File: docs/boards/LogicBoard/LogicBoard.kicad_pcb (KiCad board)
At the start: 2 copper layers, 50 x 100 mm, 7 parts, among them J1 24V IN, J2 12V OUT, U1 URB2412ZP-6WR3

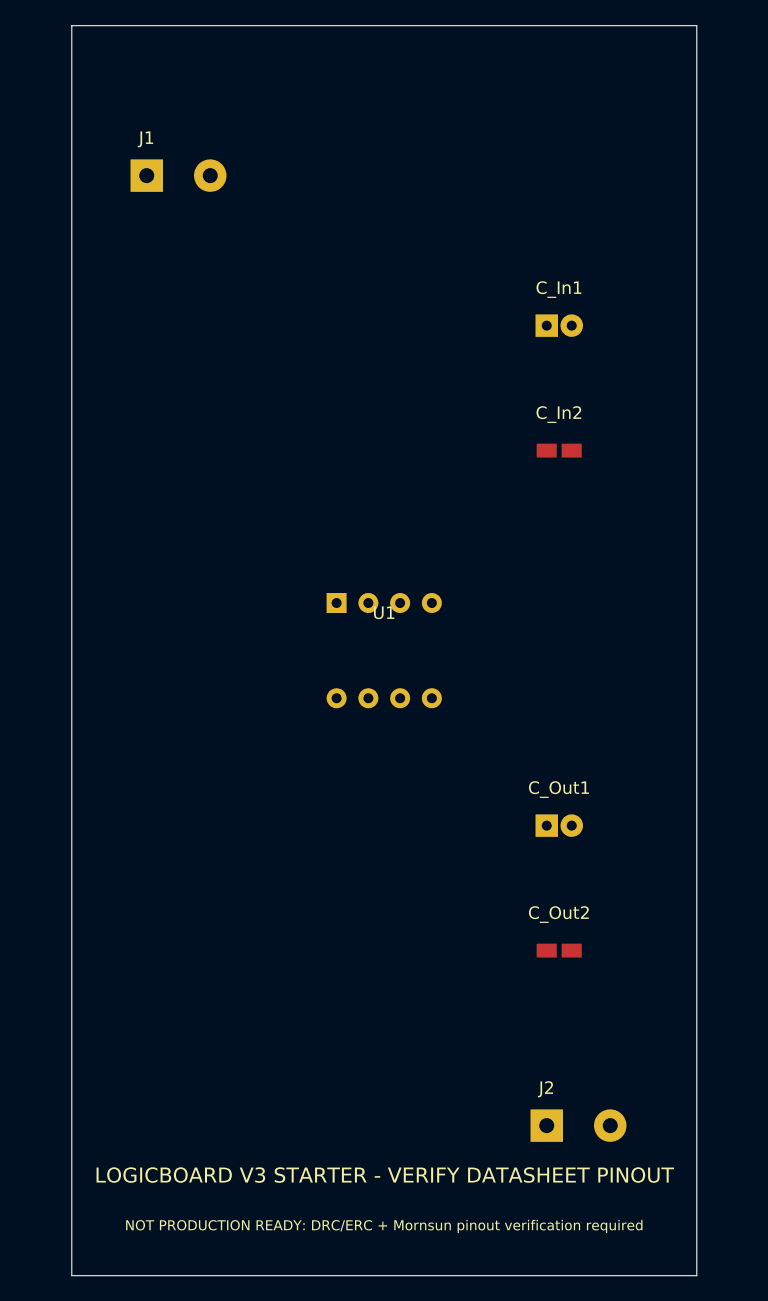
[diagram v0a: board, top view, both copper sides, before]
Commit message: Remake LogicBoard PCB to v4A functional layout
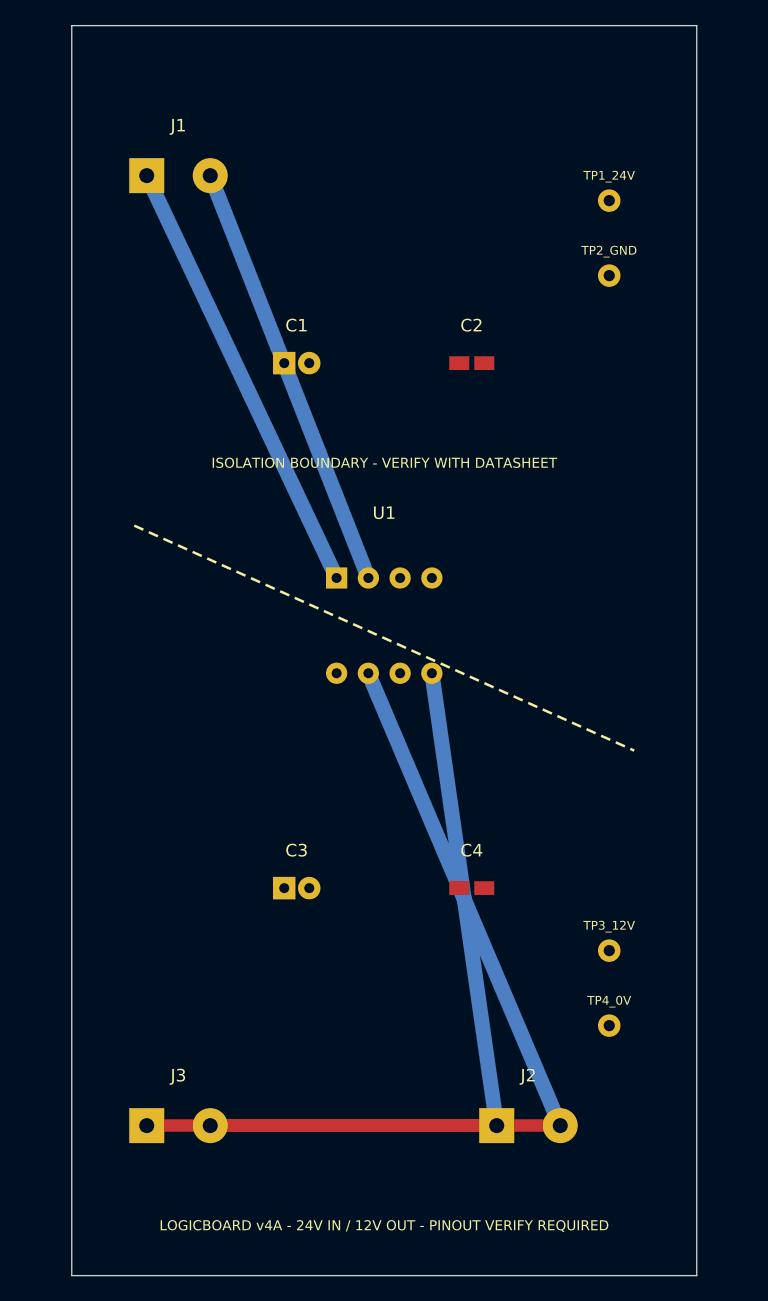
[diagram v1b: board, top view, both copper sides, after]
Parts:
- removed C_In1: 10uF/50V, Capacitor_THT:CP_Radial_D5.0mm_P2.00mm
- removed C_In2: 0.1uF/100V, Capacitor_SMD:C_1206_3216Metric
- removed C_Out1: 22uF/50V, Capacitor_THT:CP_Radial_D5.0mm_P2.00mm
- removed C_Out2: 0.1uF/50V, Capacitor_SMD:C_1206_3216Metric
- added C1: 10uF_50V, Custom:CP_D5_P2, F.Cu at (18.0, 27.0)
- added C2: 100nF, Custom:C_1206, F.Cu at (32.0, 27.0)
- added C3: 22uF_50V, Custom:CP_D5_P2, F.Cu at (18.0, 69.0)
- added C4: 100nF, Custom:C_1206, F.Cu at (32.0, 69.0)
- added J3: FAN_12V, Custom:Terminal_2P_5.08, F.Cu at (6.00, 88.0)
- added TP1_24V: , Custom:TP1mm, F.Cu at (43.0, 14.0)
- added TP2_GND: , Custom:TP1mm, F.Cu at (43.0, 20.0)
- added TP3_12V: , Custom:TP1mm, F.Cu at (43.0, 74.0)
- added TP4_0V: , Custom:TP1mm, F.Cu at (43.0, 80.0)
- J1: value 24V IN -> 24V_IN; footprint Custom:TerminalBlock_5.08mm_2P -> Custom:Terminal_2P_5.08
- J2: value 12V OUT -> 12V_OUT; footprint Custom:TerminalBlock_5.08mm_2P -> Custom:Terminal_2P_5.08
- U1: footprint Mornsun:URB2412ZP-6WR3 -> Custom:URB_ZP_6W_DIP8_VERIFY
- moved J2 4.00 mm to (34.0, 88.0)
- moved U1 2.00 mm to (25.0, 48.0)
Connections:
- net VIN renamed VIN_24V
- net VOUT renamed OUT_12V
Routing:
- net GND_OUT: track 0.00 -> 67.3 mm
- net OUT_12V: track 0.00 -> 64.6 mm
- net VIN_24V: track 0.00 -> 35.6 mm
- net GND_IN: track 0.00 -> 34.6 mm
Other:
- board text added: "ISOLATION BOUNDARY - VERIFY WITH DATASHEET"
- board text added: "LOGICBOARD v4A - 24V IN / 12V OUT - PINOUT VERIFY REQUIRED"
- board text removed: "LOGICBOARD V3 STARTER - VERIFY DATASHEET PINOUT"
- board text removed: "NOT PRODUCTION READY: DRC/ERC + Mornsun pinout verification required"

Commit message: v4C fix LogicBoard to URB ZP DIP24 footprint
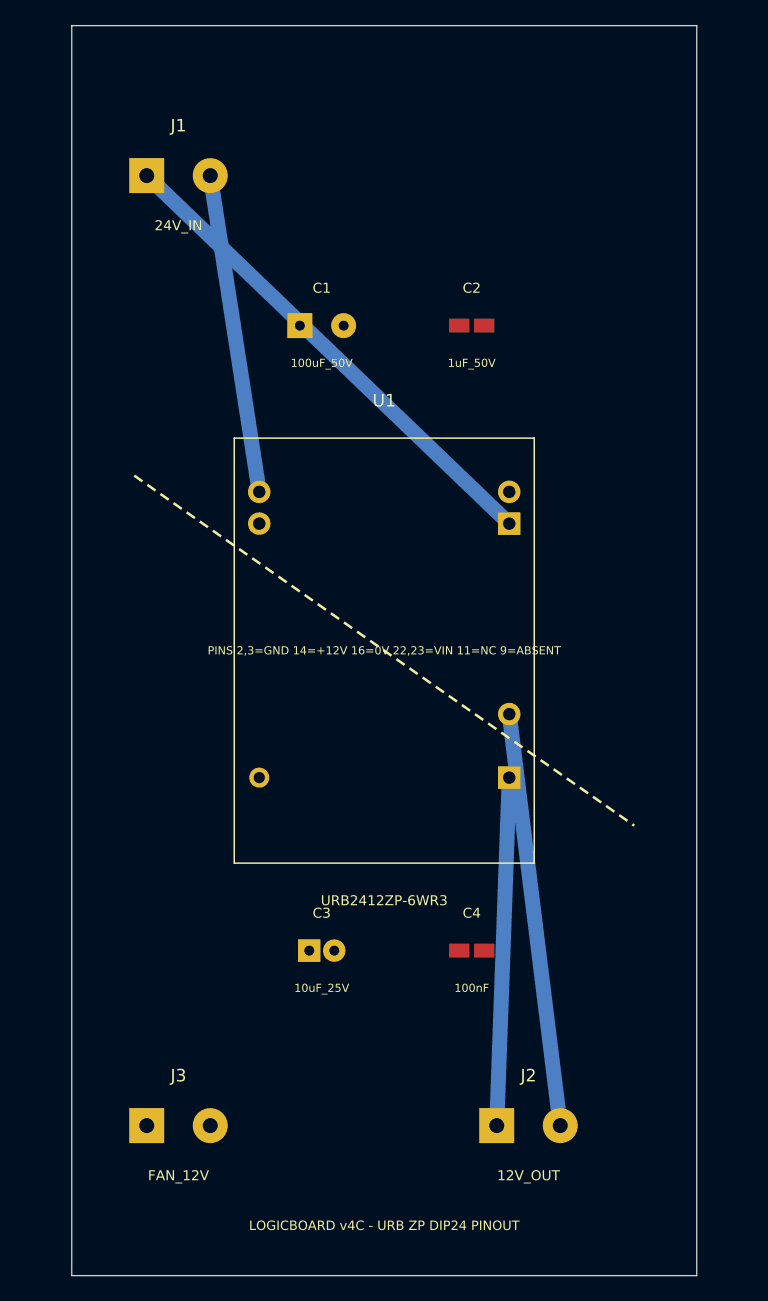
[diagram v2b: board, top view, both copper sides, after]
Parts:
- removed TP1_24V, TP2_GND, TP3_12V, TP4_0V: , Custom:TP1mm
- C1: value 10uF_50V -> 100uF_50V; footprint Custom:CP_D5_P2 -> CP_Radial
- C2: value 100nF -> 1uF_50V; footprint Custom:C_1206 -> C1206
- C3: value 22uF_50V -> 10uF_25V; footprint Custom:CP_D5_P2 -> CP_Radial
- C4: footprint Custom:C_1206 -> C1206
- J1, J2, J3: footprint Custom:Terminal_2P_5.08 -> Terminal_2P_5_08
- U1: footprint Custom:URB_ZP_6W_DIP8_VERIFY -> Mornsun_URB2412ZP_6WR3_DIP24
- moved C3 5.39 mm to (20.0, 74.0)
- moved C4 5.00 mm to (32.0, 74.0)
- moved C1 3.61 mm to (20.0, 24.0)
- moved C2 3.00 mm to (32.0, 24.0)
- moved U1 2.00 mm to (25.0, 50.0)
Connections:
- U1 pad 3: (no net) -> GND_IN
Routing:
- net OUT_12V: track 64.6 -> 27.9 mm
- net GND_OUT: track 67.3 -> 33.2 mm
- net GND_IN: track 34.6 -> 25.6 mm
- net VIN_24V: track 35.6 -> 40.2 mm
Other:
- board text added: "LOGICBOARD v4C - URB ZP DIP24 PINOUT"
- board text removed: "ISOLATION BOUNDARY - VERIFY WITH DATASHEET"
- board text removed: "LOGICBOARD v4A - 24V IN / 12V OUT - PINOUT VERIFY REQUIRED"

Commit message: v4K add LogicBoard testpoints mounting holes and polarity labels
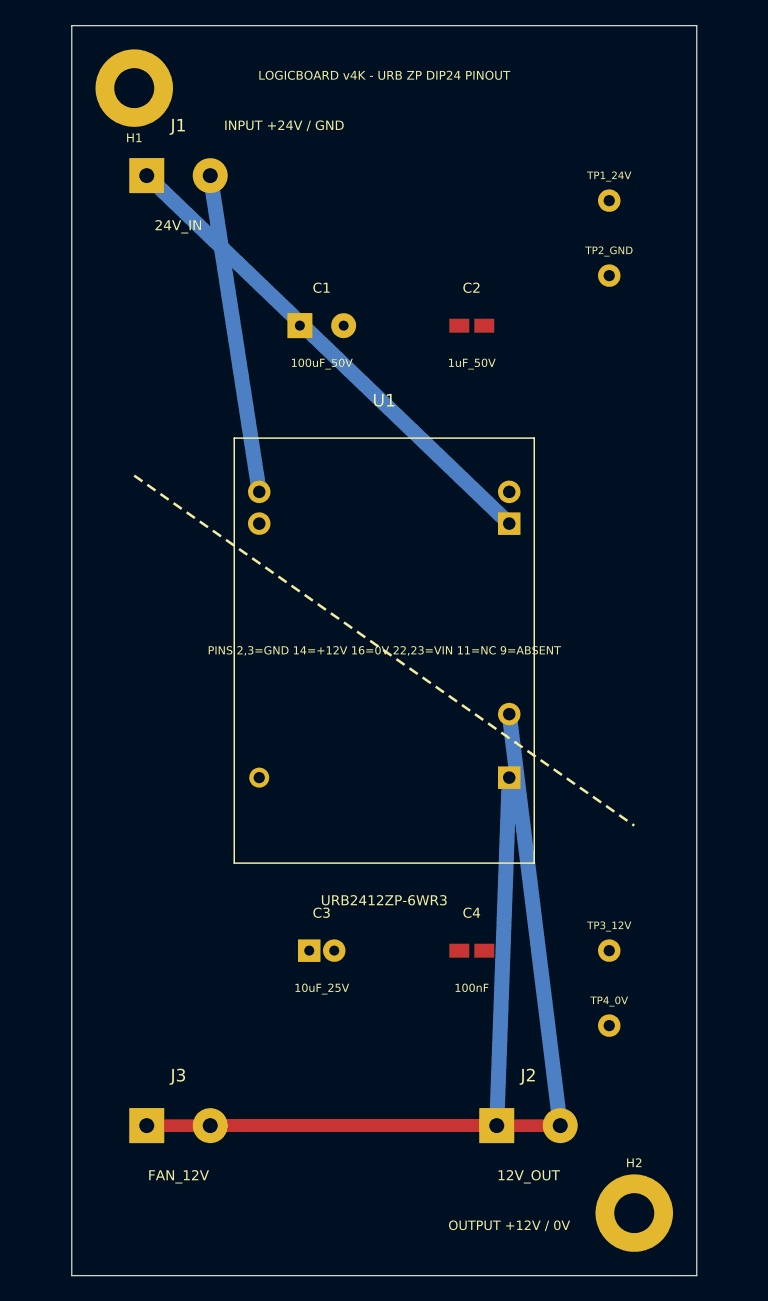
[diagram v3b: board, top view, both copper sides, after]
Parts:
- added H1: , MountingHole_M3, F.Cu at (5.00, 5.00)
- added H2: , MountingHole_M3, F.Cu at (45.0, 95.0)
- added TP1_24V: , TP1mm, F.Cu at (43.0, 14.0)
- added TP2_GND: , TP1mm, F.Cu at (43.0, 20.0)
- added TP3_12V: , TP1mm, F.Cu at (43.0, 74.0)
- added TP4_0V: , TP1mm, F.Cu at (43.0, 80.0)
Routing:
- net OUT_12V: track 27.9 -> 55.9 mm
- net GND_OUT: track 33.2 -> 61.2 mm
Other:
- board text added: "INPUT +24V / GND"
- board text added: "LOGICBOARD v4K - URB ZP DIP24 PINOUT"
- board text added: "OUTPUT +12V / 0V"
- board text removed: "LOGICBOARD v4C - URB ZP DIP24 PINOUT"
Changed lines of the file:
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@@
   (setup (pad_to_mask_clearance 0.05))
   (net 0 "") (net 1 "VIN_24V") (net 2 "GND_IN") (net 3 "OUT_12V") (net 4 "GND_OUT")
+  (footprint "MountingHole_M3" (layer "F.Cu") (at 5 5)
+    (property "Reference" "H1" (at 0 4 0) (layer "F.SilkS") (effects (font (size 0.7 0.7) (thickness 0.1))))
+    (pad "1" np_thru_hole circle (at 0 0) (size 6.2 6.2) (drill 3.2) (layers "F.Cu" "B.Cu" "F.Mask" "B.Mask"))
+  )
+  (footprint "MountingHole_M3" (layer "F.Cu") (at 45 95)
+    (property "Reference" "H2" (at 0 -4 0) (layer "F.SilkS") (effects (font (size 0.7 0.7) (thickness 0.1))))
+    (pad "1" np_thru_hole circle (at 0 0) (size 6.2 6.2) (drill 3.2) (layers "F.Cu" "B.Cu" "F.Mask" "B.Mask"))
+  )
   (footprint "Terminal_2P_5_08" (layer "F.Cu") (at 6 12)
     (property "Reference" "J1" (at 2.54 -4 0) (layer "F.SilkS") (effects (font (size 1 1) (thickness 0.15))))
@@
     (pad "2" thru_hole oval (at 5.08 0) (size 2.8 2.8) (drill 1.2) (layers "F.Cu" "B.Cu" "F.Mask" "B.Mask") (net 4 "GND_OUT"))
   )
+  (footprint "TP1mm" (layer "F.Cu") (at 43 14) (property "Reference" "TP1_24V" (at 0 -2 0) (layer "F.SilkS") (effects (font (size 0.6 0.6) (thickness 0.08)))) (pad "1" thru_hole circle (at 0 0) (size 1.8 1.8) (drill 0.9) (layers "F.Cu" "B.Cu" "F.Mask" "B.Mask") (net 1 "VIN_24V")))
+  (footprint "TP1mm" (layer "F.Cu") (at 43 20) (property "Reference" "TP2_GND" (at 0 -2 0) (layer "F.SilkS") (effects (font (size 0.6 0.6) (thickness 0.08)))) (pad "1" thru_hole circle (at 0 0) (size 1.8 1.8) (drill 0.9) (layers "F.Cu" "B.Cu" "F.Mask" "B.Mask") (net 2 "GND_IN")))
+  (footprint "TP1mm" (layer "F.Cu") (at 43 74) (property "Reference" "TP3_12V" (at 0 -2 0) (layer "F.SilkS") (effects (font (size 0.6 0.6) (thickness 0.08)))) (pad "1" thru_hole circle (at 0 0) (size 1.8 1.8) (drill 0.9) (layers "F.Cu" "B.Cu" "F.Mask" "B.Mask") (net 3 "OUT_12V")))
+  (footprint "TP1mm" (layer "F.Cu") (at 43 80) (property "Reference" "TP4_0V" (at 0 -2 0) (layer "F.SilkS") (effects (font (size 0.6 0.6) (thickness 0.08)))) (pad "1" thru_hole circle (at 0 0) (size 1.8 1.8) (drill 0.9) (layers "F.Cu" "B.Cu" "F.Mask" "B.Mask") (net 4 "GND_OUT")))
   (segment (start 6 12) (end 35 39.84) (width 1.2) (layer "B.Cu") (net 1))
   (segment (start 11.08 12) (end 15 37.3) (width 1.2) (layer "B.Cu") (net 2))
   (segment (start 35 60.16) (end 34 88) (width 1.2) (layer "B.Cu") (net 3))
   (segment (start 35 55.08) (end 39.08 88) (width 1.2) (layer "B.Cu") (net 4))
+  (segment (start 6 88) (end 34 88) (width 1.0) (layer "F.Cu") (net 3))
+  (segment (start 11.08 88) (end 39.08 88) (width 1.0) (layer "F.Cu") (net 4))
   (gr_line (start 0 0) (end 50 0) (stroke (width 0.1) (type default)) (layer "Edge.Cuts"))
   (gr_line (start 50 0) (end 50 100) (stroke (width 0.1) (type default)) (layer "Edge.Cuts"))
@@
   (gr_line (start 0 100) (end 0 0) (stroke (width 0.1) (type default)) (layer "Edge.Cuts"))
   (gr_line (start 5 36) (end 45 64) (stroke (width 0.2) (type dash)) (layer "F.SilkS"))
-  (gr_text "LOGICBOARD v4C - URB ZP DIP24 PINOUT" (at 25 96 0) (layer "F.SilkS") (effects (font (size 0.75 0.75) (thickness 0.1))))
+  (gr_text "INPUT +24V / GND" (at 17 8 0) (layer "F.SilkS") (effects (font (size 0.75 0.75) (thickness 0.1))))
+  (gr_text "OUTPUT +12V / 0V" (at 35 96 0) (layer "F.SilkS") (effects (font (size 0.75 0.75) (thickness 0.1))))
+  (gr_text "LOGICBOARD v4K - URB ZP DIP24 PINOUT" (at 25 4 0) (layer "F.SilkS") (effects (font (size 0.7 0.7) (thickness 0.1))))
 )
